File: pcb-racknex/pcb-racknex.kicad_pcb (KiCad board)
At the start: 2 copper layers, 33 x 30 mm, 15 parts, among them J1 Conn_I2C, J2 Conn_LED, J3 Conn_Fan, J4 Conn_ON_OFF, P1 Conn_Pi, Q1 S8050 NPN

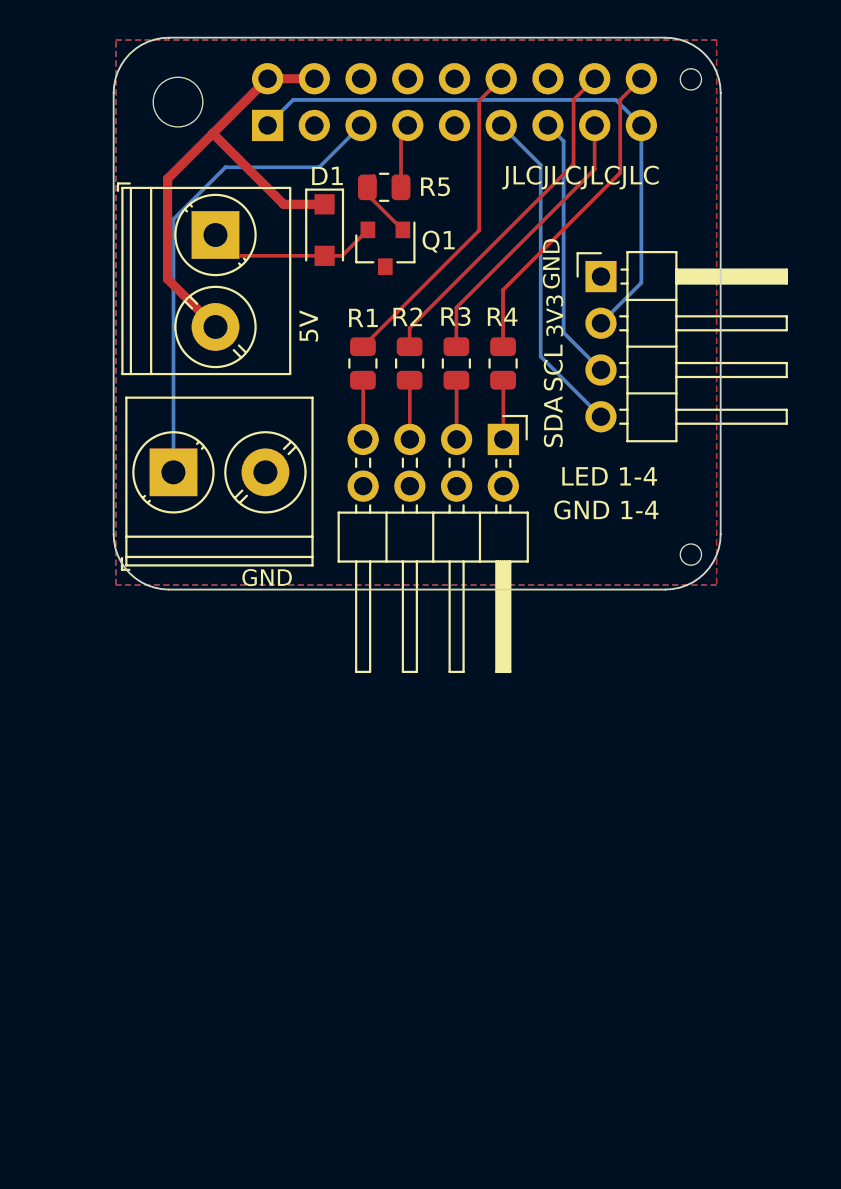
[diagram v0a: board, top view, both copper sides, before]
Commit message: Rev 2.0: added RTC
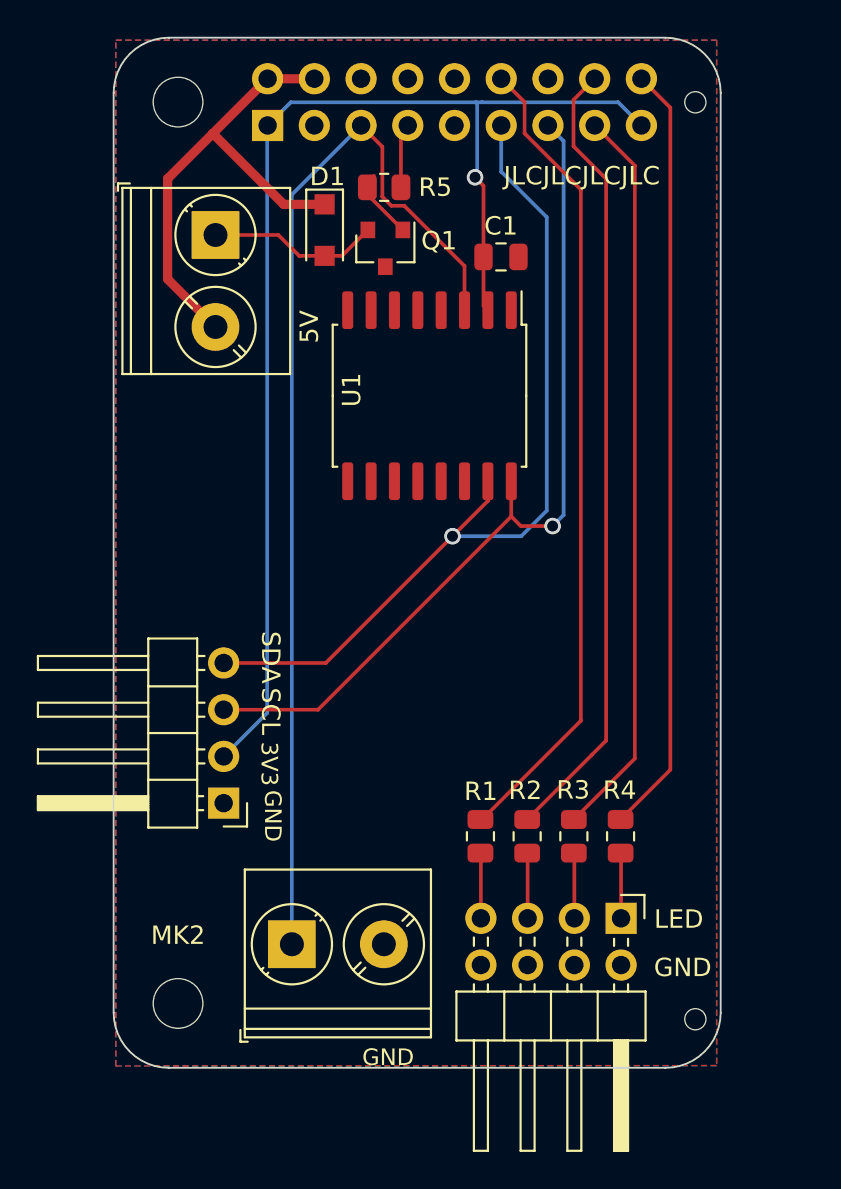
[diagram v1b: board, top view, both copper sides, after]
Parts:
- removed REF** (x2): SMT_JLCPCB_ToolingHole, user:SMT_JLCPCB_ToolingHole
- added C1: 100nF, Capacitor_SMD:C_0805_2012Metric, F.Cu at (221.1, 105.9)
- added MK2: M2.5, MountingHole:MountingHole_2.7mm_M2.5, F.Cu at (203.5, 146.5)
- added T1: 3, user:SMT_JLCPCB_ToolingHole, F.Cu at (231.6, 97.5)
- added T2: 4, user:SMT_JLCPCB_ToolingHole, F.Cu at (231.6, 147.4)
- added U1: DS3231M, Package_SO:SOIC-16W_7.5x10.3mm_P1.27mm, F.Cu at (217.2, 113.5)
- moved J1 35.2 mm to (206.0, 135.6), turned to 180 degrees
- moved J2 26.8 mm to (227.6, 141.9)
- moved R2 26.5 mm to (222.5, 137.4)
- moved R3 26.5 mm to (225.0, 137.4)
- moved R4 26.5 mm to (227.6, 137.4)
- moved R1 26.5 mm to (219.9, 137.4)
- moved J4 26.4 mm to (209.7, 143.3)
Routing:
- net +3V3: track 33.1 -> 68.3 mm, vias 0 -> 1
- net /GPIO3(ON_OFF): track 26.1 -> 58.9 mm
- net /GPIO27(SCL): track 14.5 -> 46.7 mm, vias 0 -> 1
- net /GPIO17(SDA): track 18.1 -> 46.7 mm, vias 0 -> 1
- net /GPIO18(LED): track 17.7 -> 44.4 mm
- net /GPIO22(LED): track 15.1 -> 40.0 mm
- net /GPIO23(LED): track 18.7 -> 43.3 mm
- net /GPIO24(LED): track 17.7 -> 42.0 mm
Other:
- board size 33 x 30 mm -> 33 x 56 mm
- board text added: "LED"
- board text added: "https://github.com/bablokb/pcb-racknex Rev 2.0"
- board text removed: "GND 1-4"
- board text removed: "LED 1-4"
- board text removed: "https://github.com/bablokb/pcb-racknex Rev 1.0"

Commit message: Rev 2.1: changed layout for connectors
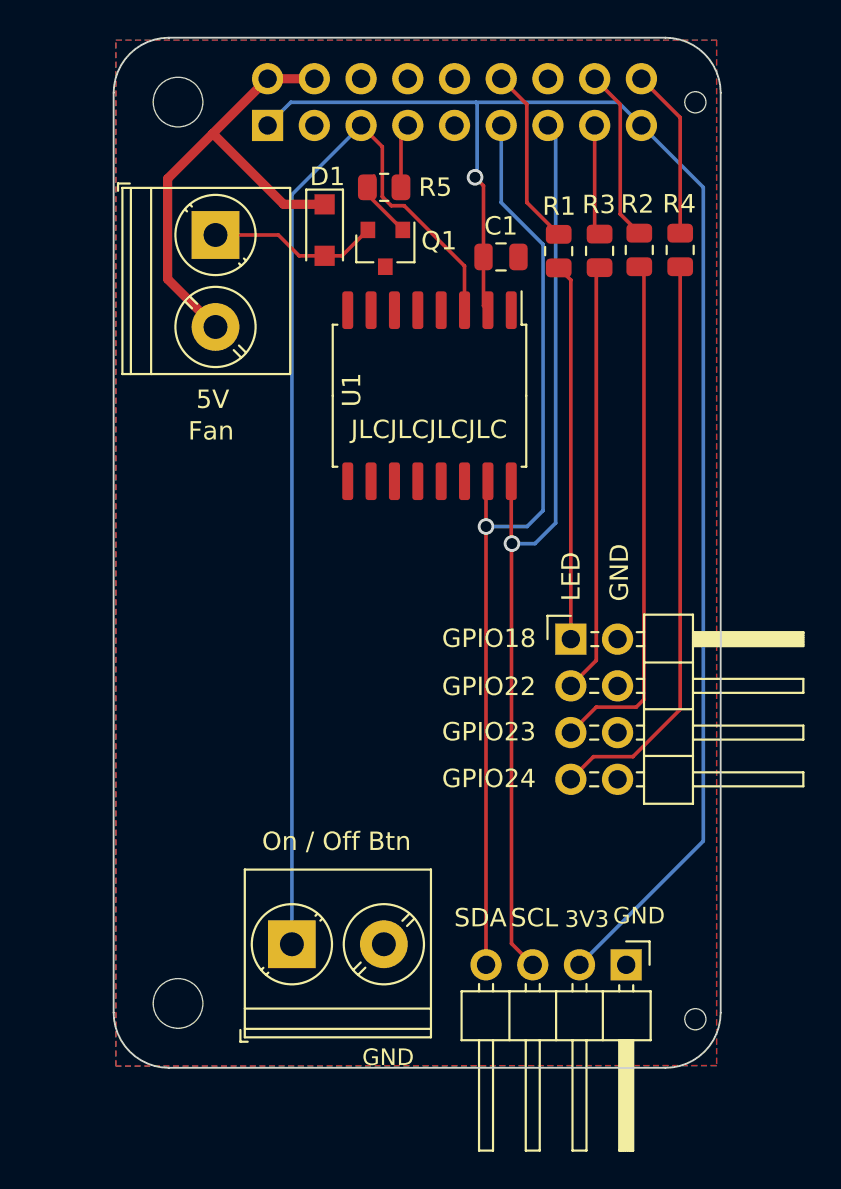
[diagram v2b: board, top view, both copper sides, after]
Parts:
- moved R2 32.5 mm to (228.6, 105.5)
- moved R1 32.1 mm to (224.2, 105.6)
- moved R4 32.0 mm to (230.8, 105.5)
- moved R3 31.9 mm to (226.4, 105.6)
- moved J1 23.6 mm to (227.9, 144.4), turned to 270 degrees
- moved J2 15.4 mm to (224.9, 126.7), turned to 0 degrees
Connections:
- R1 pad 2: Net-(J2-Pad7) -> Net-(J2-Pad1)
- R4 pad 2: Net-(J2-Pad1) -> Net-(J2-Pad7)
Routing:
- net /GPIO18(LED): track 44.4 -> 9.75 mm
- net /GPIO22(LED): track 40.0 -> 6.02 mm
- net /GPIO23(LED): track 43.3 -> 9.40 mm
- net /GPIO24(LED): track 42.0 -> 9.27 mm
- net Net-(J2-Pad7): track 3.57 -> 31.6 mm
- net Net-(J2-Pad5): track 3.57 -> 28.3 mm
- net Net-(J2-Pad3): track 3.57 -> 23.4 mm
- net Net-(J2-Pad1): track 3.57 -> 20.5 mm
- net +3V3: track 68.3 -> 82.9 mm
- net /GPIO17(SDA): track 46.7 -> 51.7 mm
- net /GPIO27(SCL): track 46.7 -> 51.4 mm
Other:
- board text added: "Fan"
- board text added: "GPIO18"
- board text added: "GPIO22"
- board text added: "GPIO23"
- board text added: "GPIO24"
- board text added: "On / Off Btn"
- board text added: "https://github.com/bablokb/pcb-racknex Rev 2.1"
- board text removed: "https://github.com/bablokb/pcb-racknex Rev 2.0"

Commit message: Rev 2.2: R-values, footprints for connectors
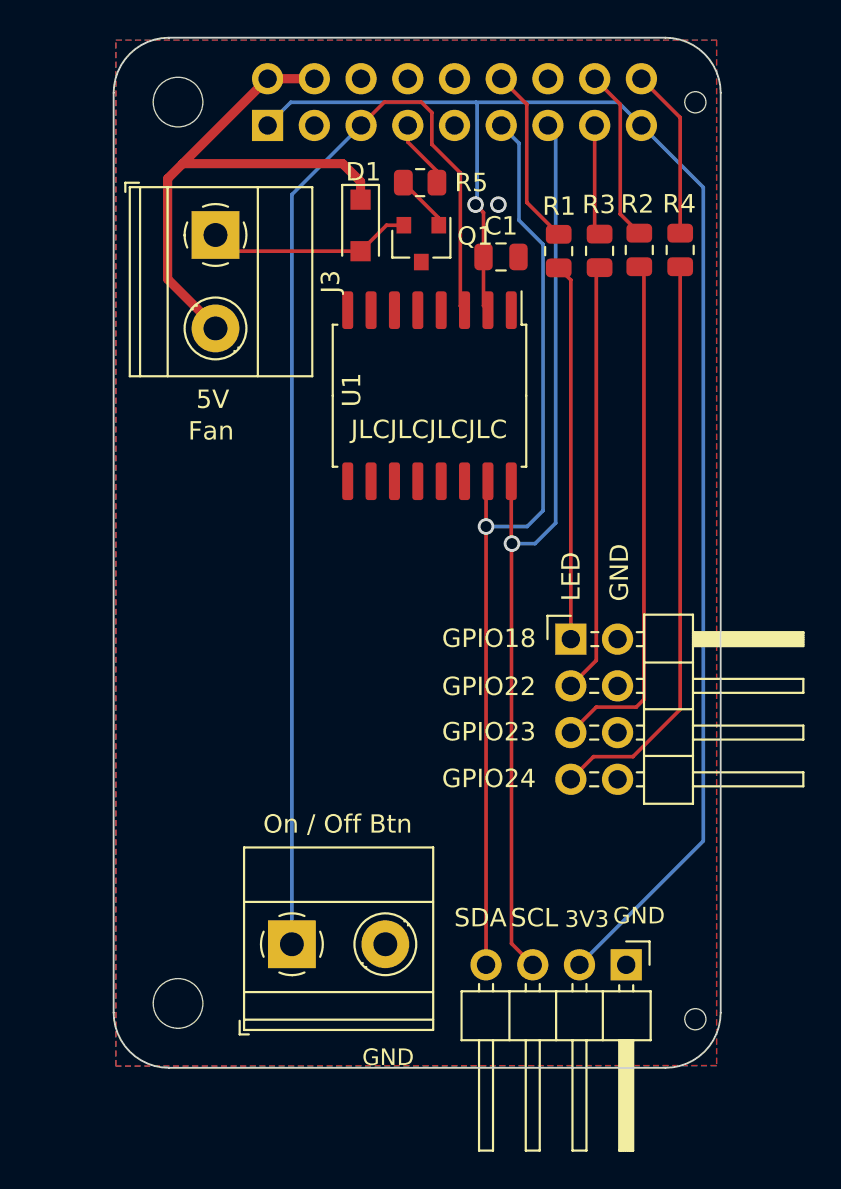
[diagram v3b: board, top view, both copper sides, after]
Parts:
- J3, J4: footprint TerminalBlock_Phoenix:TerminalBlock_Phoenix_PT-1,5-2-5.0-H_1x02_P5.00mm_Horizontal -> TerminalBlock_Phoenix:TerminalBlock_Phoenix_MKDS-1,5-2-5.08_1x02_P5.08mm_Horizontal
- R1, R2, R3, R4: value R -> 820
- R5: value R -> 3K3
- moved D1 1.97 mm to (213.4, 104.2)
- moved Q1 1.97 mm to (216.7, 105.2)
- moved R5 1.97 mm to (216.7, 101.9)
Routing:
- net +5V: track 27.0 -> 30.4 mm
- net /GPIO3(ON_OFF): track 58.9 -> 62.2 mm
- net Net-(D1-Pad2): track 9.67 -> 11.5 mm
- net /GPIO4(FAN): track 3.52 -> 4.29 mm
- net GND: vias 0 -> 1
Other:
- board text added: "https://github.com/bablokb/pcb-racknex Rev 2.2"
- board text removed: "https://github.com/bablokb/pcb-racknex Rev 2.1"

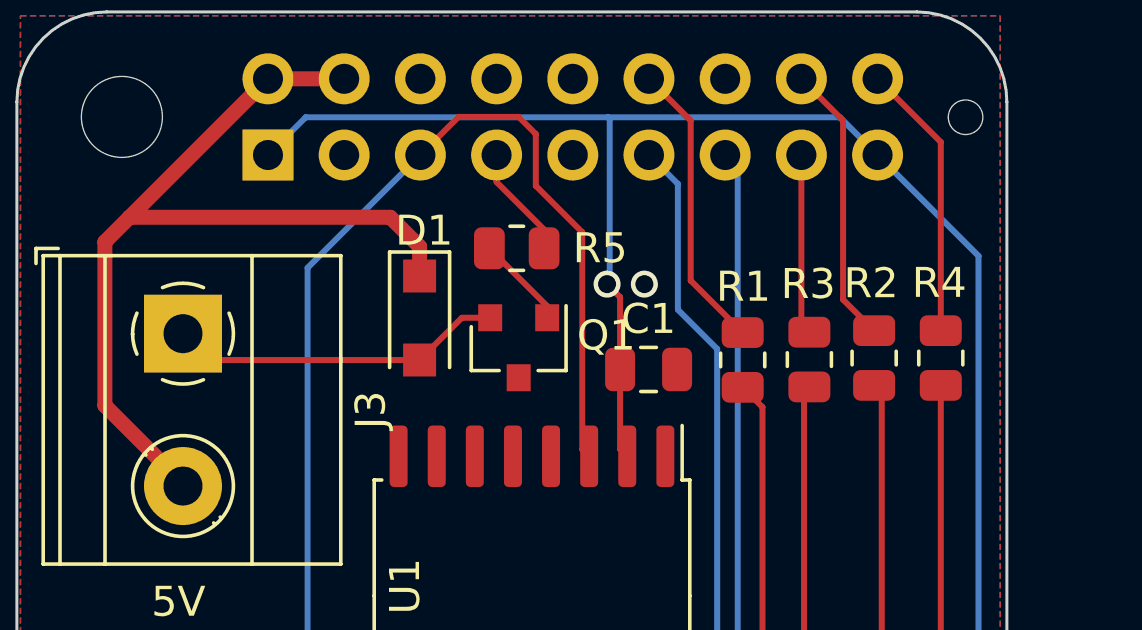
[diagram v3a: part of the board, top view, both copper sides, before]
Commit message: Rev 2.3: bugfix S8050-pins
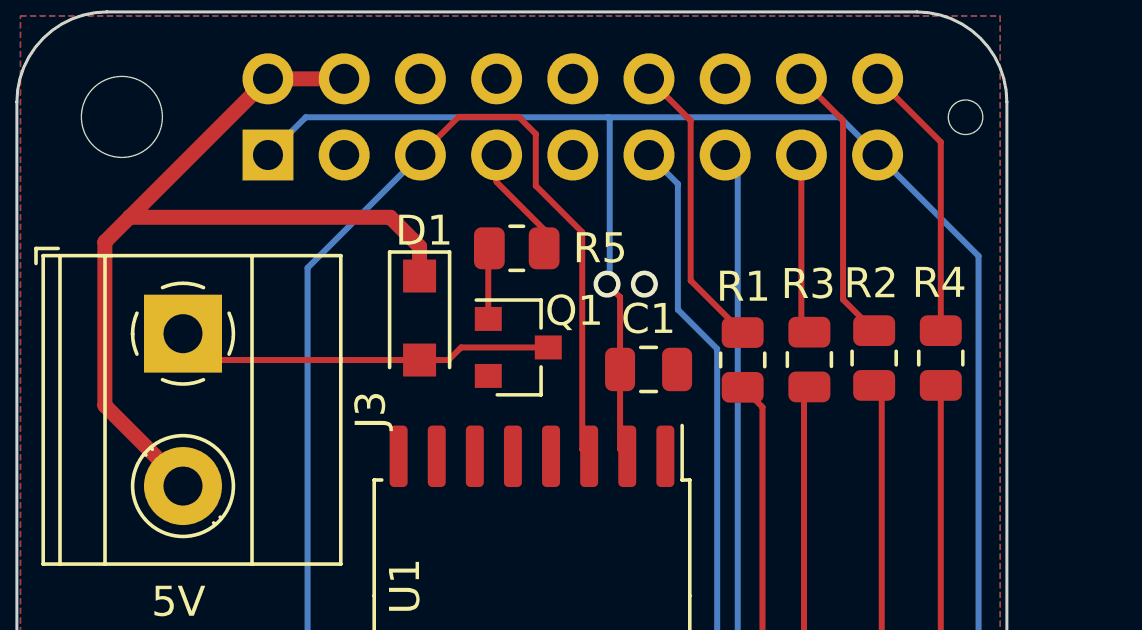
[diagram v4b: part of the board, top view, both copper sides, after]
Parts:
- turned Q1 to 0 degrees
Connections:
- Q1 pad 2: Net-(D1-Pad2) -> GND
- Q1 pad 3: GND -> Net-(D1-Pad2)
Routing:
- net Net-(D1-Pad2): track 11.5 -> 12.7 mm
- net Net-(Q1-Pad1): track 3.11 -> 2.37 mm
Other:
- board text added: "https://github.com/bablokb/pcb-racknex Rev 2.3"
- board text removed: "https://github.com/bablokb/pcb-racknex Rev 2.2"
